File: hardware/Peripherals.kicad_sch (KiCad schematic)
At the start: 27 parts, among them J3 Screw_Terminal_01x03, J4 Screw_Terminal_01x02, J5 Screw_Terminal_01x02, U7 MAX3232, U8 SP3485CN, U9 SN65HVD230

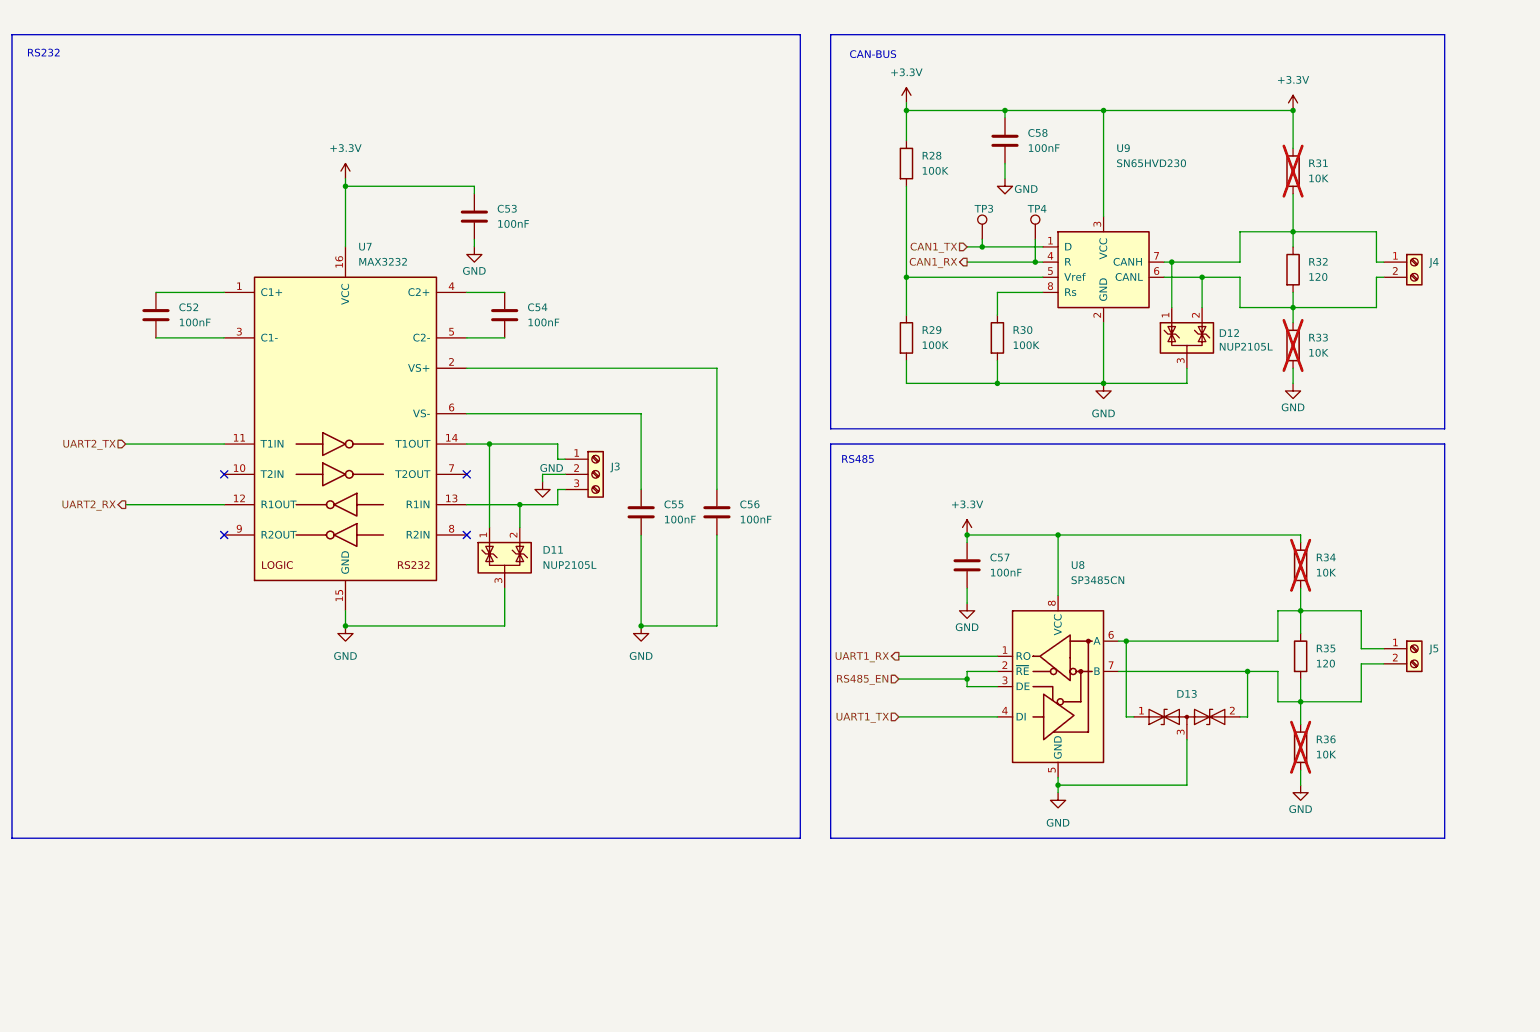
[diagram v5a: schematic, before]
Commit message: Make connectors DB9
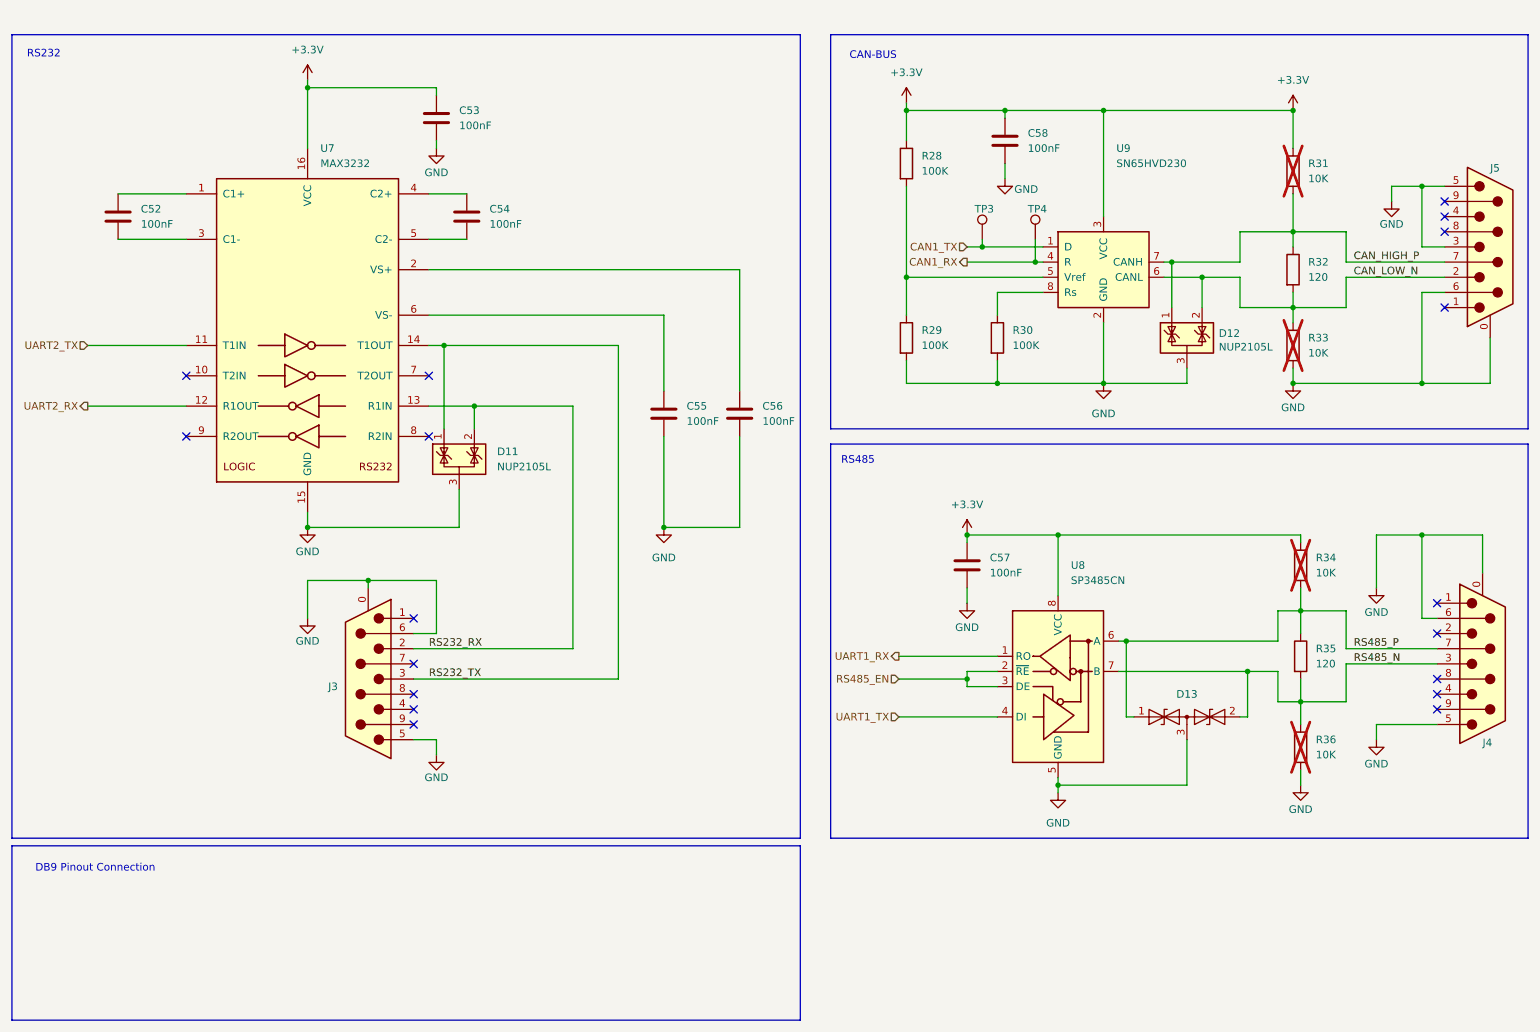
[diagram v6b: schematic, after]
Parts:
- removed J3: Screw_Terminal_01x03, TerminalBlock_Phoenix:TerminalBlock_Phoenix_MKDS-1,5-3-5.08_1x03_P5.08mm_Horizontal, symbol Connector:Screw_Terminal_01x03
- removed J4, J5: Screw_Terminal_01x02, TerminalBlock_Phoenix:TerminalBlock_Phoenix_MKDS-1,5-2-5.08_1x02_P5.08mm_Horizontal, symbol Connector:Screw_Terminal_01x02
- added J3, J4, J5: DE9_Pins_MountingHoles, Connector_Dsub:DSUB-9_Pins_Horizontal_P2.77x2.84mm_EdgePinOffset7.70mm_Housed_MountingHolesOffset9.12mm, symbol Connector:DE9_Pins_MountingHoles
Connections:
- net GND: now also J3.0 (PAD), J3.5, J3.6, J4.0 (PAD), J4.5, J4.6, J5.0 (PAD), J5.3, J5.5, J5.6
- net RS232_RX: now reaches D11.2 (K), U7.13 (R1IN)
- net RS232_RX: now also J3.2
- net RS232_TX: now reaches D11.1 (K), U7.14 (T1OUT)
- net RS232_TX: now also J3.3
- net CAN_HIGH_P: now reaches D12.1 (K), R31.2, R32.1, U9.7 (CANH)
- net CAN_HIGH_P: now also J5.7
- net CAN_LOW_N: now reaches D12.2 (K), R32.2, R33.1, U9.6 (CANL)
- net CAN_LOW_N: now also J5.2
- net RS485_P: now reaches D13.1 (A1), R34.2, R35.1, U8.6 (A)
- net RS485_P: now also J4.7
- net RS485_N: now reaches D13.2 (A2), R35.2, R36.1, U8.7 (B)
- net RS485_N: now also J4.3
- no-connect marks 4 -> 18
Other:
- note added: "DB9 Pinout Connection"
- moved on the sheet: C52, C53, C54, C55, C56, D11, U7
